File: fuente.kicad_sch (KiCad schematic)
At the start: 12 parts, among them J3 Screw_Terminal_01x02

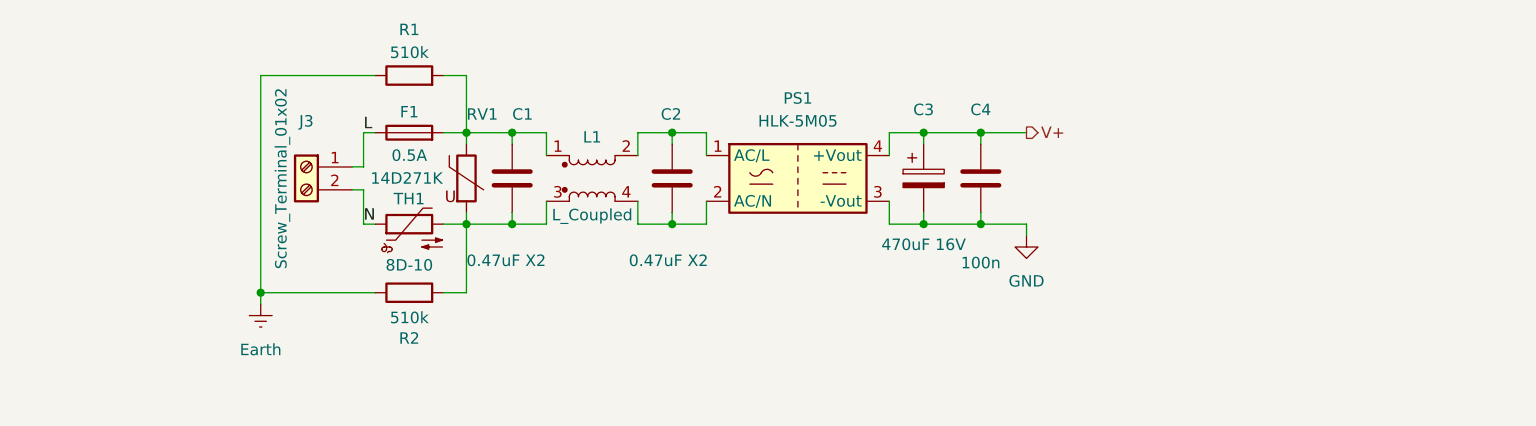
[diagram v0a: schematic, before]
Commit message: Agregar protección de sobre tensión/tensión inversa
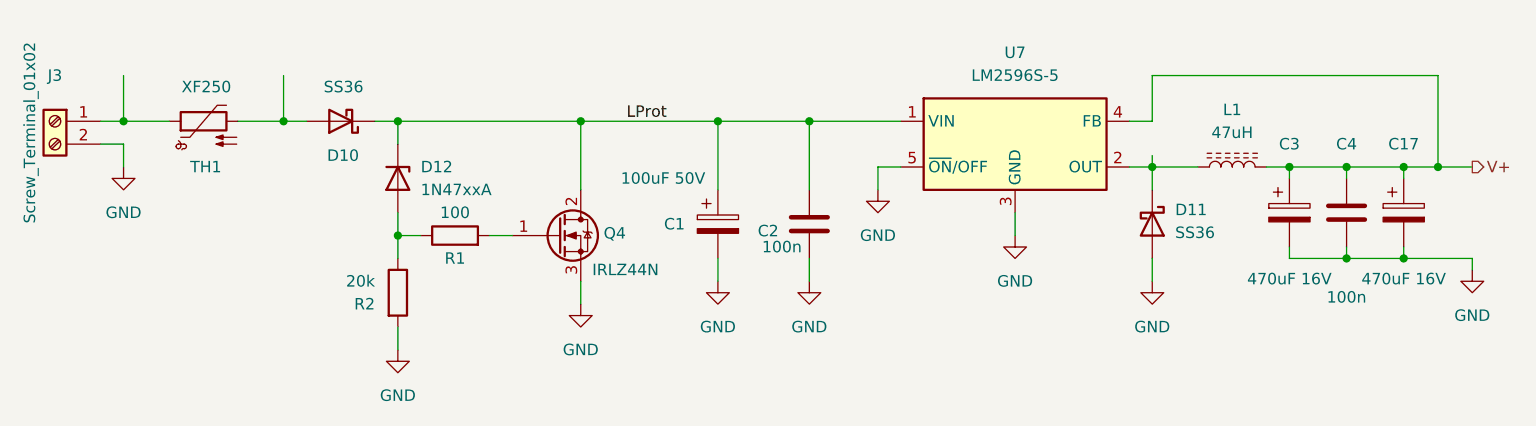
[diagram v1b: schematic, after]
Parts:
- removed C1: 0.47uF X2, Capacitor_THT:C_Rect_L18.0mm_W8.0mm_P15.00mm_FKS3_FKP3, symbol Device:C
- removed F1: 0.5A, Fuse:Fuseholder_TR5_Littelfuse_No560_No460, symbol Device:Fuse
- removed L1: L_Coupled, Inductor_THT:Choke_Schaffner_RN112-04-17.7x17.1mm, symbol Device:L_Coupled
- removed PS1: HLK-5M05, Converter_ACDC:Converter_ACDC_Hi-Link_HLK-5Mxx, symbol Converter_ACDC:HLK-5M05
- removed RV1: 14D271K, Capacitor_THT:C_Disc_D14.5mm_W5.0mm_P7.50mm, symbol Device:Varistor
- removed TH1: 8D-10, Capacitor_THT:C_Disc_D14.5mm_W5.0mm_P7.50mm, symbol Device:Thermistor_NTC
- added C1: 100uF 50V, Capacitor_THT:CP_Radial_D10.0mm_P5.00mm, symbol Device:C_Polarized
- added C17: 470uF 16V, Capacitor_THT:CP_Radial_D10.0mm_P5.00mm, symbol Device:C_Polarized
- added D10, D11: SS36, Diode_SMD:D_SMC, symbol Diode:SS36
- added D12: 1N47xxA, Diode_THT:D_DO-41_SOD81_P10.16mm_Horizontal, symbol Diode:1N47xxA
- added L1: 47uH, Inductor_SMD:L_Bourns_SRR1260, symbol Device:L_Ferrite
- added Q4: IRLZ44N, Package_TO_SOT_THT:TO-220-3_Horizontal_TabDown, symbol Transistor_FET:IRLZ44N
- added TH1: XF250, Fuse:Fuse_BelFuse_0ZRE0125FF_L21.2mm_W5.3mm, symbol Device:Thermistor_PTC
- added U7: LM2596S-5, Package_TO_SOT_SMD:TO-263-5_TabPin3, symbol Regulator_Switching:LM2596S-5
- C2: value 0.47uF X2 -> 100n; footprint Capacitor_THT:C_Rect_L18.0mm_W8.0mm_P15.00mm_FKS3_FKP3 -> Capacitor_SMD:C_0805_2012Metric
- R1: value 510k -> 100; footprint Resistor_SMD:R_1206_3216Metric -> Resistor_SMD:R_0805_2012Metric
- R2: value 510k -> 20k; footprint Resistor_SMD:R_1206_3216Metric -> Resistor_SMD:R_0805_2012Metric
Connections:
- net N is gone; now on net GND: J3.2 (Pin_2)
- net GND: now also C2.2, R2.2, C1.2, C17.2, D11.2 (A), Q4.3 (S), U7.3 (GND), U7.5 (~{ON}/OFF)
- net V+: now also C17.1, L1.2, U7.4 (FB)
- net at R1.2: now also Q4.1 (G)
- net LProt: now reaches C2.1
- net LProt: now also C1.1, D10.1 (K), D12.1 (K), Q4.2 (D), U7.1 (VIN)
- net Earth: no longer names the net of R1.1, R2.1
- net Earth: now also D12.2 (A)
- net L: no longer names the net of J3.1 (Pin_1)
- net L: now also TH1.1
- new net: D11.1 (K), L1.1, U7.2 (OUT)
- new net: D10.2 (A), TH1.2
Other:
- moved on the sheet: C3, C4
